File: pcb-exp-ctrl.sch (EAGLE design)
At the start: 5 parts, among them IC1 SAA1064, IC2 TINY13-20PU

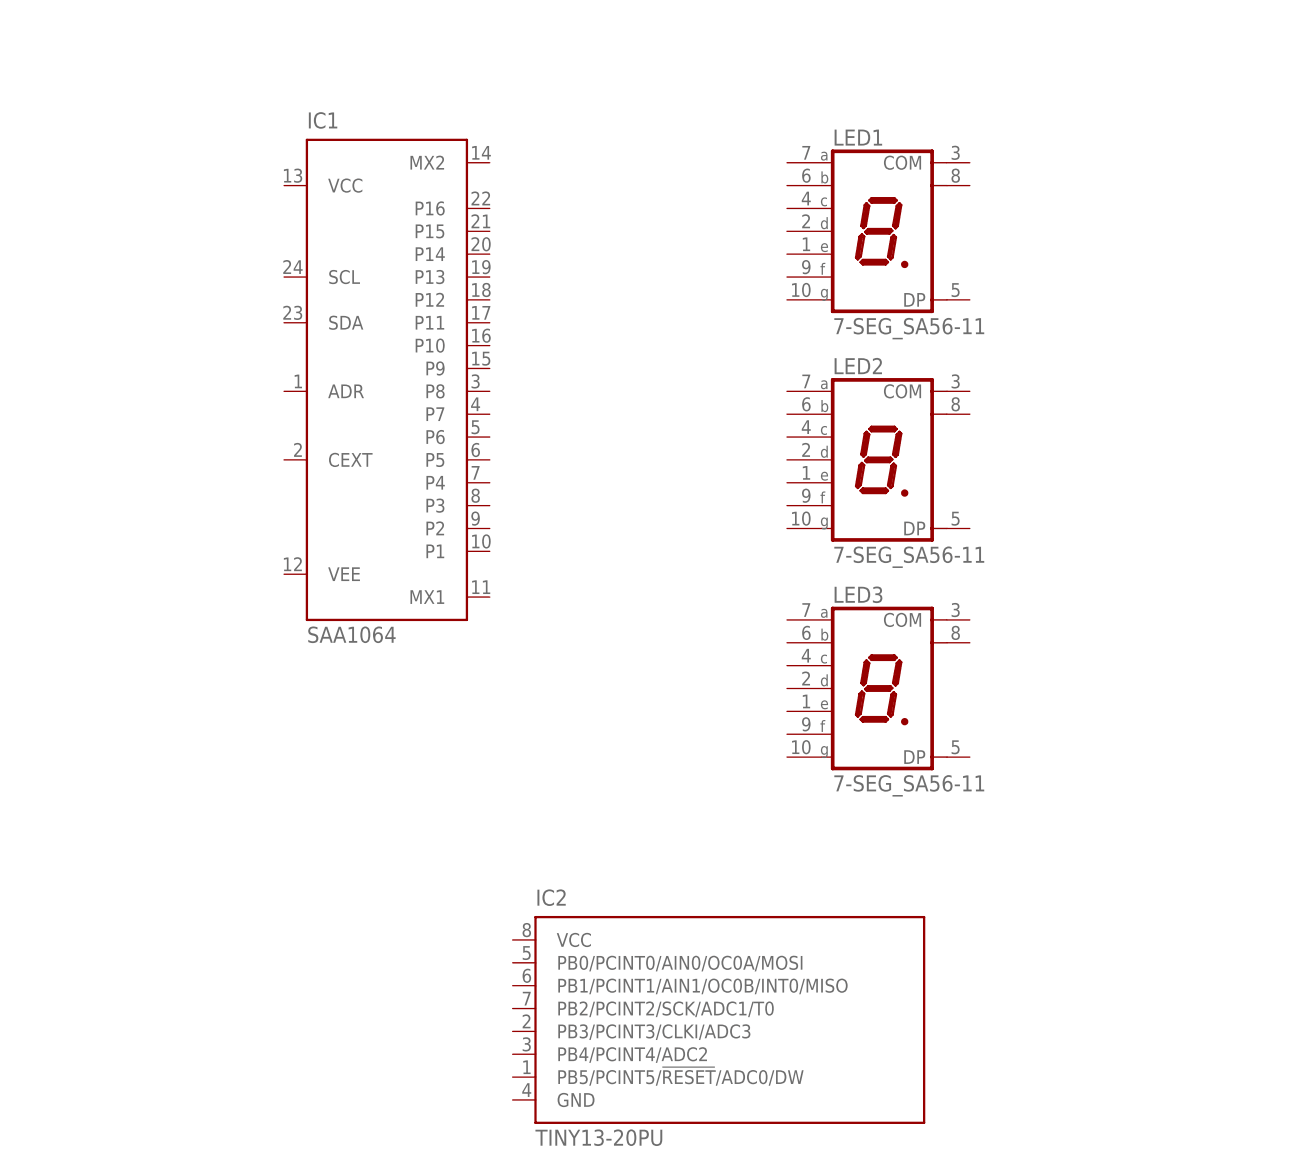
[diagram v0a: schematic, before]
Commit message: connect saa1064
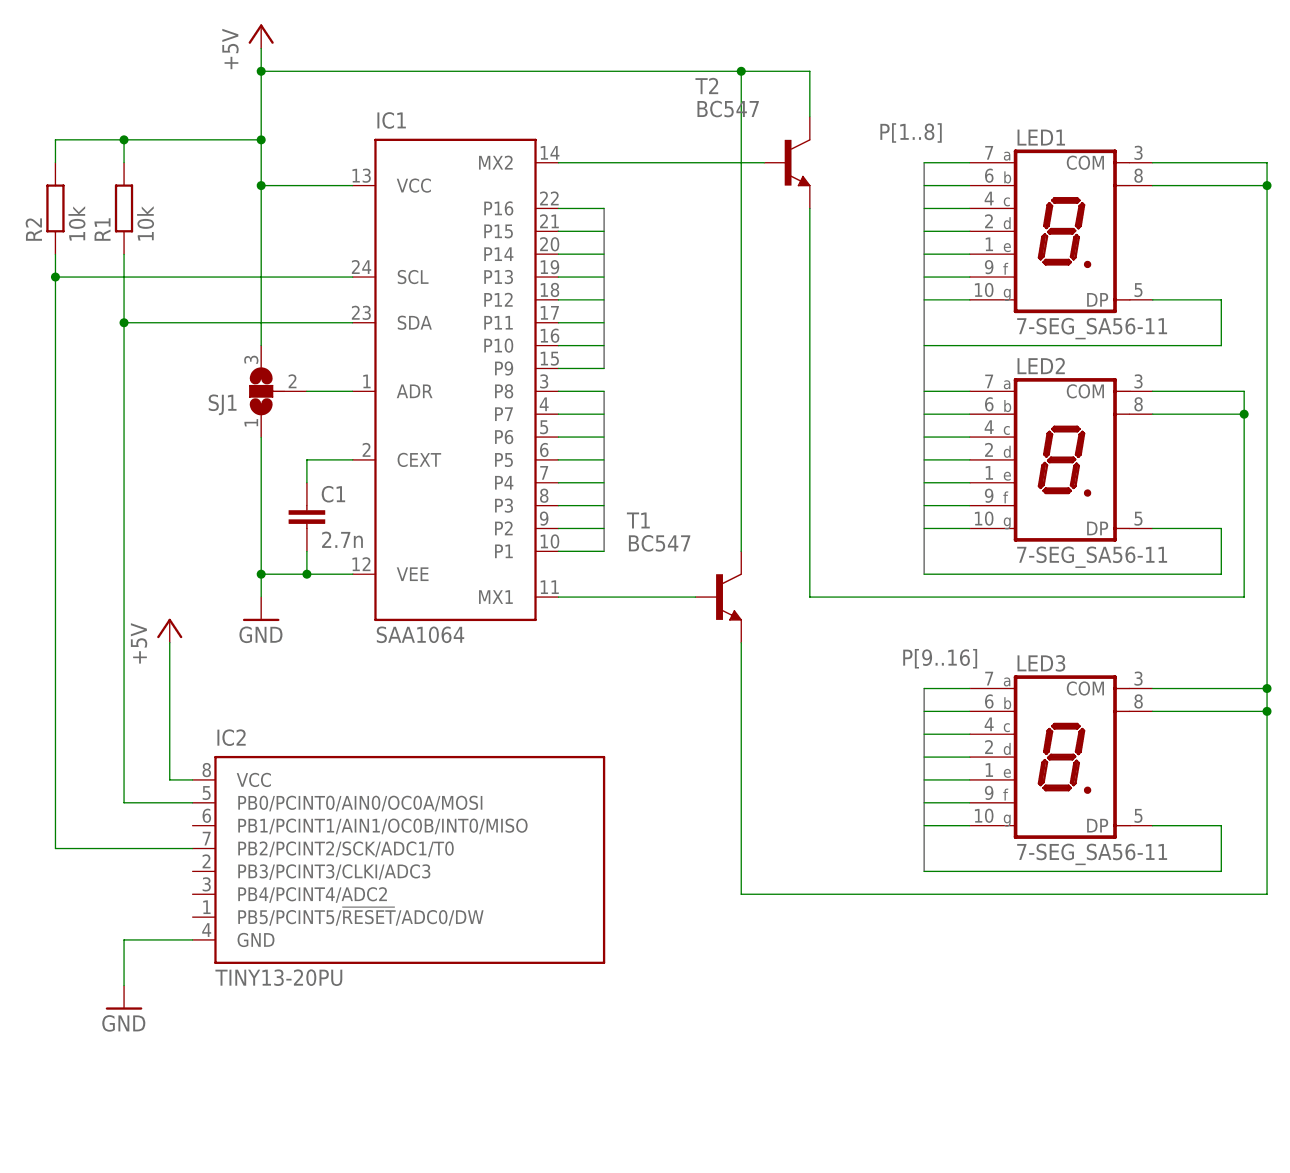
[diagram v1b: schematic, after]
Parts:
- added C1: 2.7n, rcl:C-EU025-025X050
- added R1, R2: 10k, rcl:R-EU_0204/7
- added SJ1: (no value), jumper:SJ2W
- added T1, T2: BC547, transistor:BC547
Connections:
- new net +5V: IC1.VCC, IC2.VCC, R1.2, R2.2, SJ1.3, T1.C, T2.C
- new net GND: C1.2, IC1.VEE, IC2.GND, SJ1.1
- new net N$1: IC1.SCL, IC2.PB2/PCINT2/SCK/ADC1/T0, R2.1
- new net N$10: IC1.MX2, T2.B
- new net N$2: LED2.COM@1, LED2.COM@2, T2.E
- new net N$3: IC1.SDA, IC2.PB0/PCINT0/AIN0/OC0A/MOSI, R1.1
- new net N$5: C1.1, IC1.CEXT
- new net N$6: IC1.ADR, SJ1.2
- new net N$7: LED1.COM@1, LED1.COM@2, LED3.COM@1, LED3.COM@2, T1.E
- new net N$8: IC1.MX1, T1.B
- new net P1: IC1.P1, LED1.A, LED2.A
- new net P10: IC1.P10, LED3.B
- new net P11: IC1.P11, LED3.C
- new net P12: IC1.P12, LED3.D
- new net P13: IC1.P13, LED3.E
- new net P14: IC1.P14, LED3.F
- new net P15: IC1.P15, LED3.G
- new net P16: IC1.P16, LED3.DP
- new net P2: IC1.P2, LED1.B, LED2.B
- new net P3: IC1.P3, LED1.C, LED2.C
- new net P4: IC1.P4, LED1.D, LED2.D
- new net P5: IC1.P5, LED1.E, LED2.E
- new net P6: IC1.P6, LED1.F, LED2.F
- new net P7: IC1.P7, LED1.G, LED2.G
- new net P8: IC1.P8, LED1.DP, LED2.DP
- new net P9: IC1.P9, LED3.A
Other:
- moved on the sheet: IC1, IC2, LED1, LED2, LED3

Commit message: add 100n capacities for ICs
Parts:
- added C2, C3: 100n, rcl:C-EU025-025X050
- added R3: 10k, rcl:R-EU_0204/7
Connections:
- new net N$11: IC2.PB5/PCINT5/!RESET!/ADC0/DW, R3.1
- net +5V: now also C2.1, C3.1, R3.2
- net GND: now also C2.2, C3.2
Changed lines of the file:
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@@
 <part name="T2" library="transistor" deviceset="BC547" device=""/>
 <part name="T1" library="transistor" deviceset="BC547" device=""/>
+<part name="C2" library="rcl" deviceset="C-EU" device="025-025X050" value="100n"/>
+<part name="C3" library="rcl" deviceset="C-EU" device="025-025X050" value="100n"/>
+<part name="R3" library="rcl" deviceset="R-EU_" device="0204/7" value="10k"/>
 </parts>
 <sheets>
@@
 <instance part="LED2" gate="G$1" x="88.9" y="55.88"/>
 <instance part="LED3" gate="G$1" x="88.9" y="22.86"/>
-<instance part="GND1" gate="1" x="-15.24" y="-5.08"/>
+<instance part="GND1" gate="1" x="-40.64" y="-5.08"/>
 <instance part="GND2" gate="1" x="0" y="38.1"/>
-<instance part="P+1" gate="1" x="0" y="104.14"/>
-<instance part="P+2" gate="1" x="-10.16" y="38.1"/>
+<instance part="P+1" gate="1" x="-7.62" y="104.14"/>
+<instance part="P+2" gate="1" x="-40.64" y="38.1"/>
 <instance part="SJ1" gate="G$1" x="0" y="63.5" rot="R180"/>
 <instance part="R1" gate="G$1" x="-15.24" y="83.82" rot="R90"/>
@@
 <instance part="T2" gate="G$1" x="58.42" y="88.9"/>
 <instance part="T1" gate="G$1" x="50.8" y="40.64"/>
+<instance part="C2" gate="G$1" x="-7.62" y="50.8"/>
+<instance part="C3" gate="G$1" x="-40.64" y="12.7"/>
+<instance part="R3" gate="G$1" x="-27.94" y="12.7" rot="R90"/>
 </instances>
 <busses>
@@
 <pinref part="GND1" gate="1" pin="GND"/>
 <pinref part="IC2" gate="G$1" pin="GND"/>
-<wire x1="-15.24" y1="-2.54" x2="-15.24" y2="2.54" width="0.1524" layer="91"/>
-<wire x1="-15.24" y1="2.54" x2="-7.62" y2="2.54" width="0.1524" layer="91"/>
+<wire x1="-40.64" y1="-2.54" x2="-40.64" y2="2.54" width="0.1524" layer="91"/>
+<wire x1="-40.64" y1="2.54" x2="-7.62" y2="2.54" width="0.1524" layer="91"/>
+<pinref part="C3" gate="G$1" pin="2"/>
+<wire x1="-40.64" y1="7.62" x2="-40.64" y2="2.54" width="0.1524" layer="91"/>
+<junction x="-40.64" y="2.54"/>
 </segment>
 <segment>
@@
 <wire x1="5.08" y1="45.72" x2="5.08" y2="43.18" width="0.1524" layer="91"/>
 <junction x="5.08" y="43.18"/>
+<pinref part="C2" gate="G$1" pin="2"/>
+<wire x1="0" y1="43.18" x2="-7.62" y2="43.18" width="0.1524" layer="91"/>
+<wire x1="-7.62" y1="43.18" x2="-7.62" y2="45.72" width="0.1524" layer="91"/>
 </segment>
 </net>
@@
 <segment>
 <pinref part="P+1" gate="1" pin="+5V"/>
-<pinref part="IC1" gate="G$1" pin="VCC"/>
-<wire x1="0" y1="101.6" x2="0" y2="99.06" width="0.1524" layer="91"/>
-<wire x1="0" y1="99.06" x2="0" y2="91.44" width="0.1524" layer="91"/>
-<wire x1="0" y1="91.44" x2="0" y2="86.36" width="0.1524" layer="91"/>
-<wire x1="0" y1="86.36" x2="10.16" y2="86.36" width="0.1524" layer="91"/>
-<pinref part="SJ1" gate="G$1" pin="3"/>
-<wire x1="0" y1="68.58" x2="0" y2="86.36" width="0.1524" layer="91"/>
-<junction x="0" y="86.36"/>
-<pinref part="R1" gate="G$1" pin="2"/>
-<wire x1="-15.24" y1="88.9" x2="-15.24" y2="91.44" width="0.1524" layer="91"/>
-<wire x1="-15.24" y1="91.44" x2="0" y2="91.44" width="0.1524" layer="91"/>
-<wire x1="-15.24" y1="91.44" x2="-22.86" y2="91.44" width="0.1524" layer="91"/>
-<pinref part="R2" gate="G$1" pin="2"/>
-<wire x1="-22.86" y1="91.44" x2="-22.86" y2="88.9" width="0.1524" layer="91"/>
-<junction x="-15.24" y="91.44"/>
-<junction x="0" y="91.44"/>
+<wire x1="-7.62" y1="101.6" x2="-7.62" y2="99.06" width="0.1524" layer="91"/>
 <pinref part="T2" gate="G$1" pin="C"/>
 <wire x1="60.96" y1="93.98" x2="60.96" y2="99.06" width="0.1524" layer="91"/>
@@
 <pinref part="T1" gate="G$1" pin="C"/>
 <wire x1="53.34" y1="99.06" x2="0" y2="99.06" width="0.1524" layer="91"/>
+<wire x1="0" y1="99.06" x2="-7.62" y2="99.06" width="0.1524" layer="91"/>
 <wire x1="53.34" y1="45.72" x2="53.34" y2="99.06" width="0.1524" layer="91"/>
 <junction x="53.34" y="99.06"/>
+<junction x="-7.62" y="99.06"/>
+<pinref part="C2" gate="G$1" pin="1"/>
+<wire x1="-7.62" y1="53.34" x2="-7.62" y2="99.06" width="0.1524" layer="91"/>
+<pinref part="R2" gate="G$1" pin="2"/>
+<pinref part="R1" gate="G$1" pin="2"/>
+<wire x1="-15.24" y1="88.9" x2="-15.24" y2="99.06" width="0.1524" layer="91"/>
+<wire x1="-15.24" y1="99.06" x2="-22.86" y2="99.06" width="0.1524" layer="91"/>
+<wire x1="-22.86" y1="99.06" x2="-22.86" y2="88.9" width="0.1524" layer="91"/>
+<wire x1="-7.62" y1="99.06" x2="-15.24" y2="99.06" width="0.1524" layer="91"/>
+<pinref part="IC1" gate="G$1" pin="VCC"/>
+<wire x1="0" y1="86.36" x2="10.16" y2="86.36" width="0.1524" layer="91"/>
+<pinref part="SJ1" gate="G$1" pin="3"/>
+<wire x1="0" y1="68.58" x2="0" y2="86.36" width="0.1524" layer="91"/>
+<wire x1="0" y1="86.36" x2="0" y2="99.06" width="0.1524" layer="91"/>
+<junction x="-15.24" y="99.06"/>
 <junction x="0" y="99.06"/>
+<junction x="0" y="86.36"/>
 </segment>
 <segment>
 <pinref part="P+2" gate="1" pin="+5V"/>
 <pinref part="IC2" gate="G$1" pin="VCC"/>
-<wire x1="-10.16" y1="35.56" x2="-10.16" y2="20.32" width="0.1524" layer="91"/>
-<wire x1="-10.16" y1="20.32" x2="-7.62" y2="20.32" width="0.1524" layer="91"/>
+<wire x1="-40.64" y1="35.56" x2="-40.64" y2="20.32" width="0.1524" layer="91"/>
+<wire x1="-40.64" y1="20.32" x2="-27.94" y2="20.32" width="0.1524" layer="91"/>
+<pinref part="C3" gate="G$1" pin="1"/>
+<wire x1="-27.94" y1="20.32" x2="-7.62" y2="20.32" width="0.1524" layer="91"/>
+<wire x1="-40.64" y1="15.24" x2="-40.64" y2="20.32" width="0.1524" layer="91"/>
+<junction x="-40.64" y="20.32"/>
+<pinref part="R3" gate="G$1" pin="2"/>
+<wire x1="-27.94" y1="17.78" x2="-27.94" y2="20.32" width="0.1524" layer="91"/>
+<junction x="-27.94" y="20.32"/>
 </segment>
 </net>
@@
 </segment>
 </net>
+<net name="N$11" class="0">
+<segment>
+<pinref part="IC2" gate="G$1" pin="PB5/PCINT5/!RESET!/ADC0/DW"/>
+<wire x1="-7.62" y1="5.08" x2="-27.94" y2="5.08" width="0.1524" layer="91"/>
+<pinref part="R3" gate="G$1" pin="1"/>
+<wire x1="-27.94" y1="5.08" x2="-27.94" y2="7.62" width="0.1524" layer="91"/>
+</segment>
+</net>
